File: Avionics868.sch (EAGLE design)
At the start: 69 parts, among them SW1 B3U-1000P-2P-SMD, U1 ATSAMD21G18_QFN, U2 SPX3819M5-L-3-0, U3 MCP73831T-2ACI/OT, U4 MPU-9250, U5 SIM868, U6 BMP280, X1 JSTPH, X2 32.768, X3 ZX62-B-5PA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

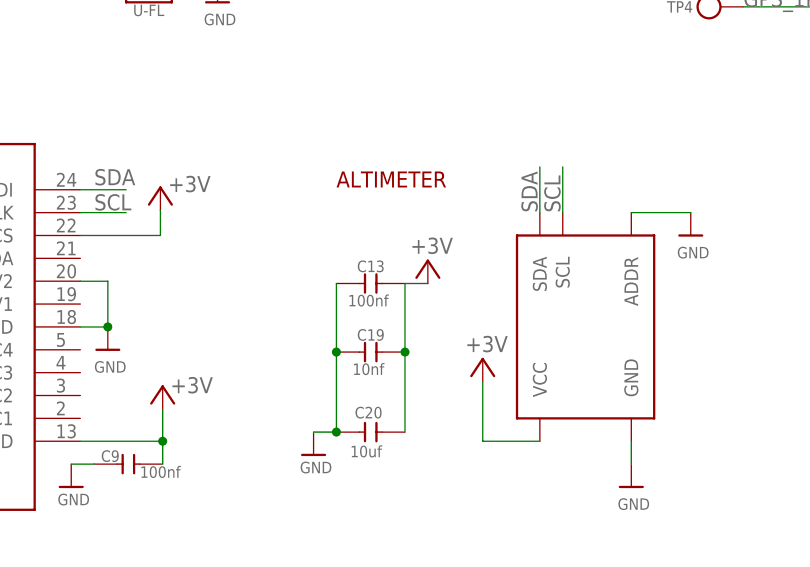
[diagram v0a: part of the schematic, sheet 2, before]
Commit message: Moved things around to improve capacitor placement
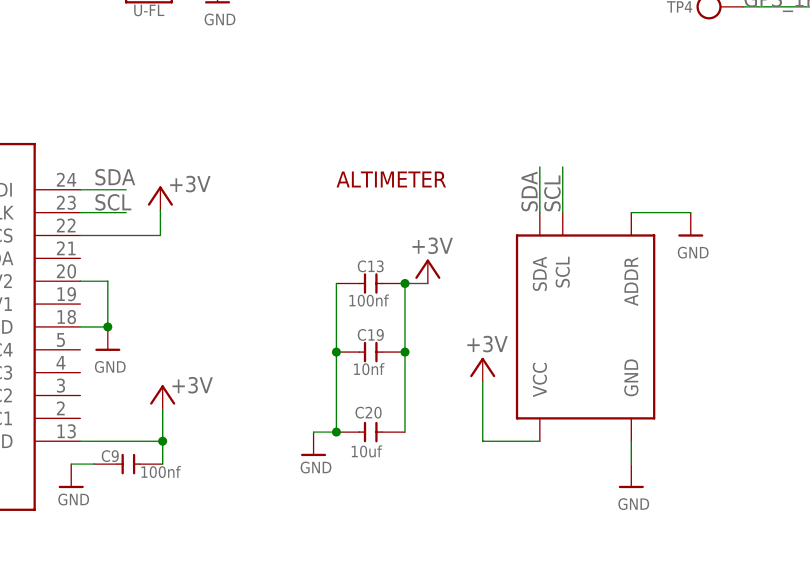
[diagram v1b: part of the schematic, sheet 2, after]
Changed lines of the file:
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@@
 <wire x1="104.648" y1="26.416" x2="104.648" y2="35.306" width="0.1524" layer="91"/>
 <junction x="104.648" y="35.306"/>
+<junction x="104.648" y="42.926"/>
 </segment>
 <segment>

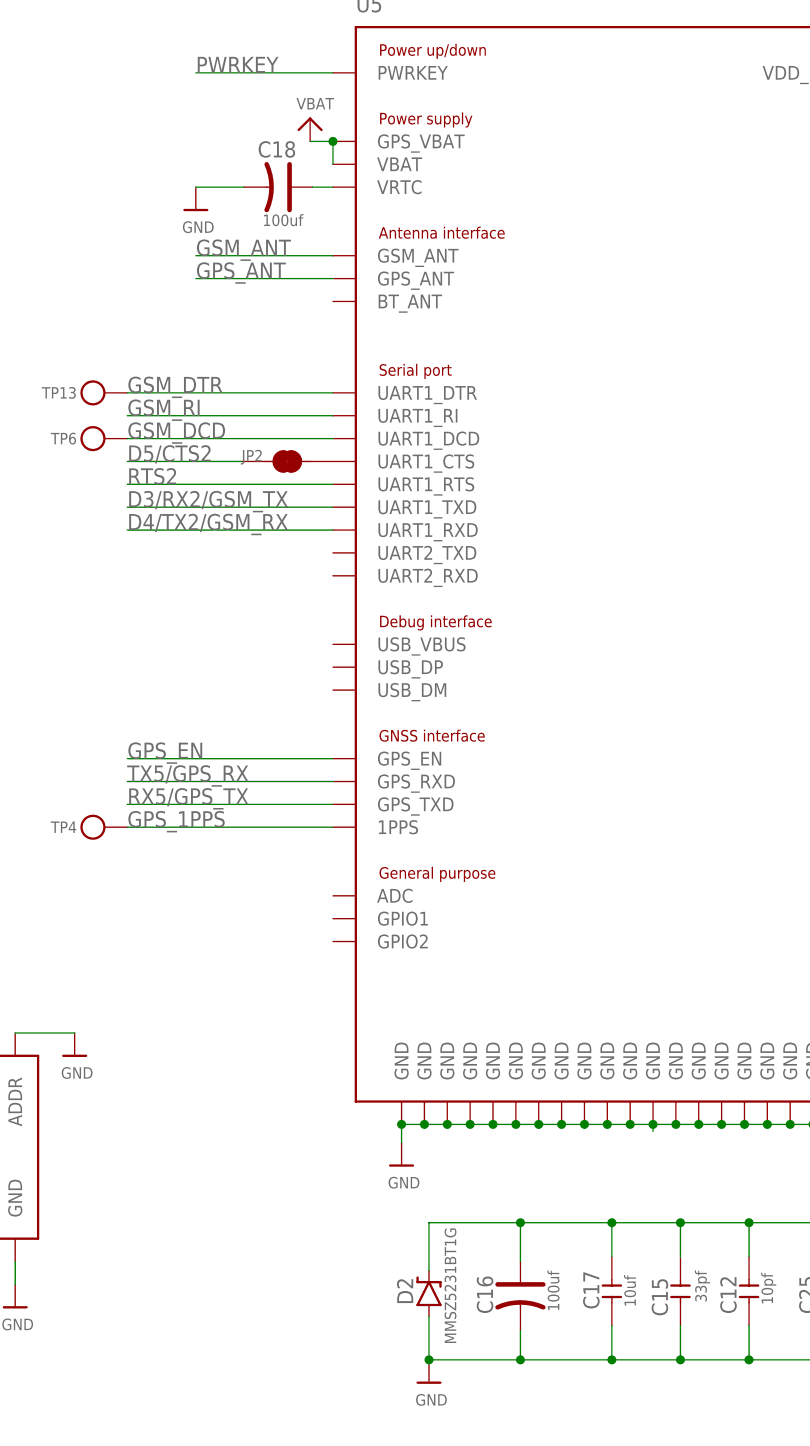
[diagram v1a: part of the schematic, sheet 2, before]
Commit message: Switched Tantanum AVX-B caps with Ceramic C1206
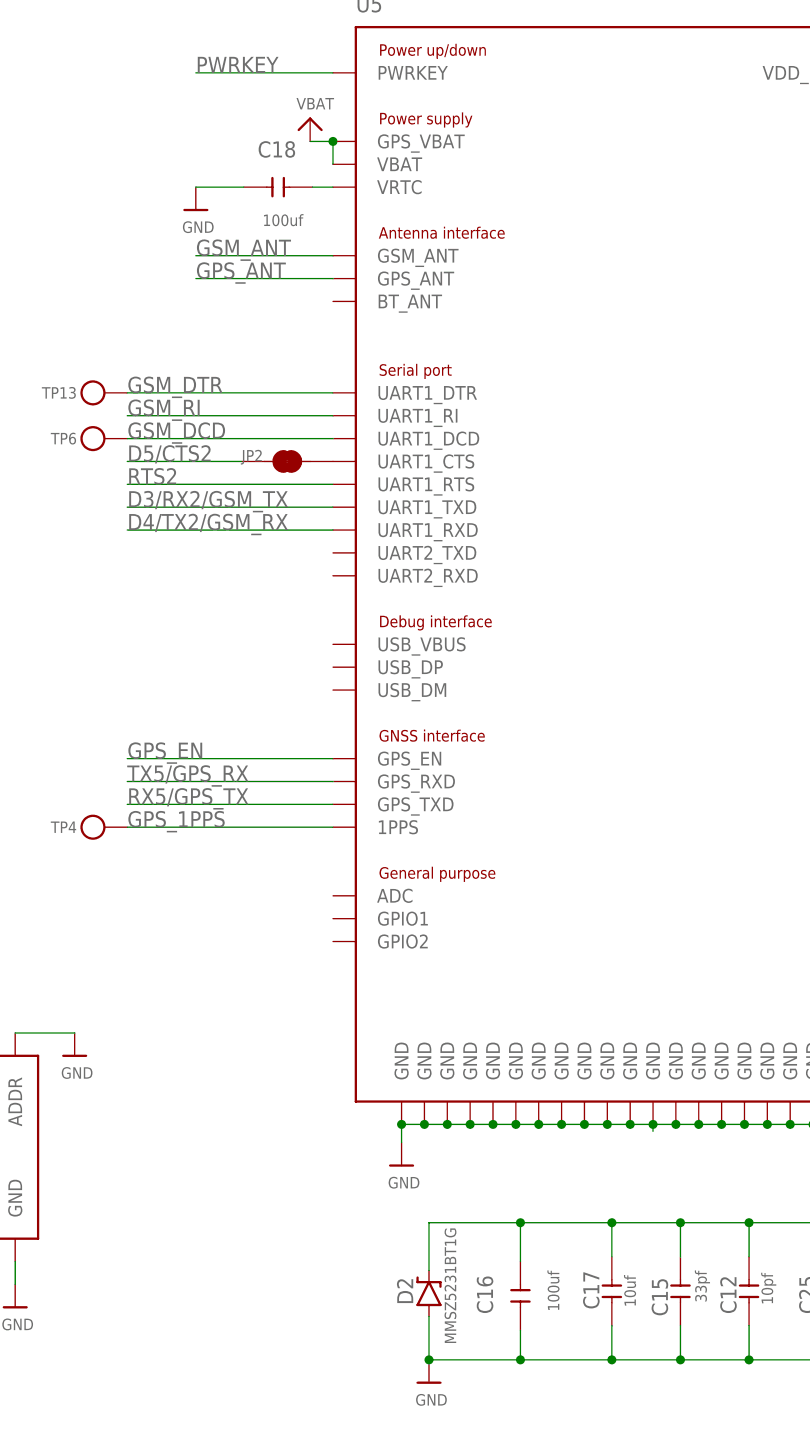
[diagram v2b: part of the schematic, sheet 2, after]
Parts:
- C16, C18: device Seeed-Capacitor-2016:TANTALUM-SMD-100UF-10V(AVX-B) -> Seeed-Capacitor-2016:CERAMIC-100UF-6.3V-20%-X5R(1206)
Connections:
- net GND: now also C16.2, C18.2; no longer C16.-, C18.-
- net N$29: now also C18.1; no longer C18.+
- net VBAT: now also C16.1; no longer C16.+
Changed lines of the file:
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@@
 <part name="C12" library="Seeed-Capacitor-2016" deviceset="CERAMIC-10PF-50V-5%-NPO(0603)" device="" value="10pf"/>
 <part name="C15" library="Custom" deviceset="CERAMIC-33PF-50V-5%-NPO(0603)" device="" value="33pf"/>
-<part name="C16" library="Seeed-Capacitor-2016" deviceset="TANTALUM-SMD-100UF-10V(AVX-B)" device="" value="100uf"/>
+<part name="C16" library="Seeed-Capacitor-2016" deviceset="CERAMIC-100UF-6.3V-20%-X5R(1206)" device="" value="100uf"/>
 <part name="C17" library="Seeed-Capacitor-2016" deviceset="CERAMIC-10UF-10V-10%-X5R(0603)" device="" value="10uf"/>
 <part name="U5" library="SIM868" deviceset="SIM868" device=""/>
@@
 <part name="U$43" library="microbuilder" deviceset="GND" device=""/>
 <part name="U$48" library="microbuilder" deviceset="GND" device=""/>
-<part name="C18" library="Seeed-Capacitor-2016" deviceset="TANTALUM-SMD-100UF-10V(AVX-B)" device="" value="100uf"/>
+<part name="C18" library="Seeed-Capacitor-2016" deviceset="CERAMIC-100UF-6.3V-20%-X5R(1206)" device="" value="100uf"/>
 <part name="JP2" library="SparkFun-Passives" deviceset="JUMPER-PAD-2-NC_BY_TRACE" device=""/>
 <part name="TP5" library="microbuilder" deviceset="TESTPOINT" device="ROUND1.5MM"/>
@@
 <pinref part="U$37" gate="G$1" pin="GND"/>
 <wire x1="155.194" y1="144.78" x2="149.86" y2="144.78" width="0.1524" layer="91"/>
-<pinref part="C18" gate="G$1" pin="-"/>
+<pinref part="C18" gate="G$1" pin="2"/>
 </segment>
 <segment>
@@
 <segment>
 <wire x1="185.928" y1="14.478" x2="185.928" y2="17.78" width="0.1524" layer="91"/>
-<pinref part="C16" gate="G$1" pin="-"/>
+<pinref part="C16" gate="G$1" pin="2"/>
 <wire x1="196.088" y1="14.478" x2="185.928" y2="14.478" width="0.1524" layer="91"/>
 <pinref part="C17" gate="G$1" pin="2"/>
@@
 <pinref part="U5" gate="G$1" pin="VRTC"/>
 <wire x1="165.1" y1="144.78" x2="162.814" y2="144.78" width="0.1524" layer="91"/>
-<pinref part="C18" gate="G$1" pin="+"/>
+<pinref part="C18" gate="G$1" pin="1"/>
 </segment>
 </net>
@@
 </segment>
 <segment>
-<pinref part="C16" gate="G$1" pin="+"/>
+<pinref part="C16" gate="G$1" pin="1"/>
 <wire x1="185.928" y1="25.4" x2="185.928" y2="29.718" width="0.1524" layer="91"/>
 <wire x1="185.928" y1="29.718" x2="196.088" y2="29.718" width="0.1524" layer="91"/>
